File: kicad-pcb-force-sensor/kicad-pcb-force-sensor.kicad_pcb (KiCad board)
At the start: 2 copper layers, 68.6 x 53.3 mm, 24 parts, among them J1 Power, J2 Digital/PWM, J3 Analog, J4 Digital/PWM, U3 KY-040

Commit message: Servo
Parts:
- added M1: Motor_Servo, graphite_emprunts:Servo, F.Cu at (104.0, 50.9)
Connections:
- J2 pad 9: /D9 -> D9 PWM

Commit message: Avec pistes
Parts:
- removed R2: 1k, Resistor_THT:R_Axial_DIN0204_L3.6mm_D1.6mm_P7.62mm_Horizontal
- AOP1: value LTC1050HS8_PBF -> LTC1050
- Rflex1: value 23k -> 47k
- moved Flex_sensor1 52.3 mm to (157.3, 90.6), turned to -90 degrees
- moved U1 46.3 mm to (145.3, 59.0), turned to 0 degrees
- moved Pot_Digital1 41.7 mm to (113.9, 66.1), turned to -90 degrees
- moved Rflex1 41.3 mm to (151.0, 73.6), turned to 90 degrees
- moved M1 29.3 mm to (132.0, 59.5), turned to 180 degrees
- moved C2 25.7 mm to (139.2, 81.5)
- moved R6 24.4 mm to (145.5, 72.7), turned to -90 degrees
- moved Graphite_sensor1 23.9 mm to (137.0, 93.5)
- moved C1 22.7 mm to (134.8, 81.5), turned to 180 degrees
- moved R1 22.4 mm to (126.4, 86.5)
- moved C4 21.0 mm to (137.8, 72.0), turned to 180 degrees
- moved AOP1 20.9 mm to (122.5, 74.5), turned to 90 degrees
- moved U3 20.8 mm to (159.0, 61.7), turned to -90 degrees
- moved R5 18.8 mm to (138.6, 90.0), turned to 180 degrees
- moved R3 8.77 mm to (130.2, 77.0)
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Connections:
- J2 pad 8: D10 PWM/MOSI -> D10 PWM/SS
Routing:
- net VCC: track 0.00 -> 214.4 mm
- net R2: track 0.00 -> 48.4 mm
- net D11 PWM/MOSI: track 0.00 -> 34.7 mm
- net Net-(AOP1-OUT): track 0.00 -> 33.7 mm
- net Flex: track 0.00 -> 29.1 mm
- net DT: track 0.00 -> 26.6 mm
- net ADC: track 0.00 -> 23.6 mm
- net Net-(AOP1-+IN): track 0.00 -> 20.8 mm
- net D10 PWM/SS: track 0.00 -> 20.2 mm
- net D13 PWM/SCK: track 0.00 -> 15.9 mm
- net SCL: track 0.00 -> 15.7 mm
- net GND: track 0.00 -> 13.9 mm
- net SW: track 0.00 -> 13.6 mm
- net D9 PWM: track 0.00 -> 12.3 mm
- net TXD: track 0.00 -> 11.8 mm
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- added copper zone on B.Cu, net GND
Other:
- board size 68.6 x 53.3 mm -> 68.8 x 55 mm
- board text added: "SCL"

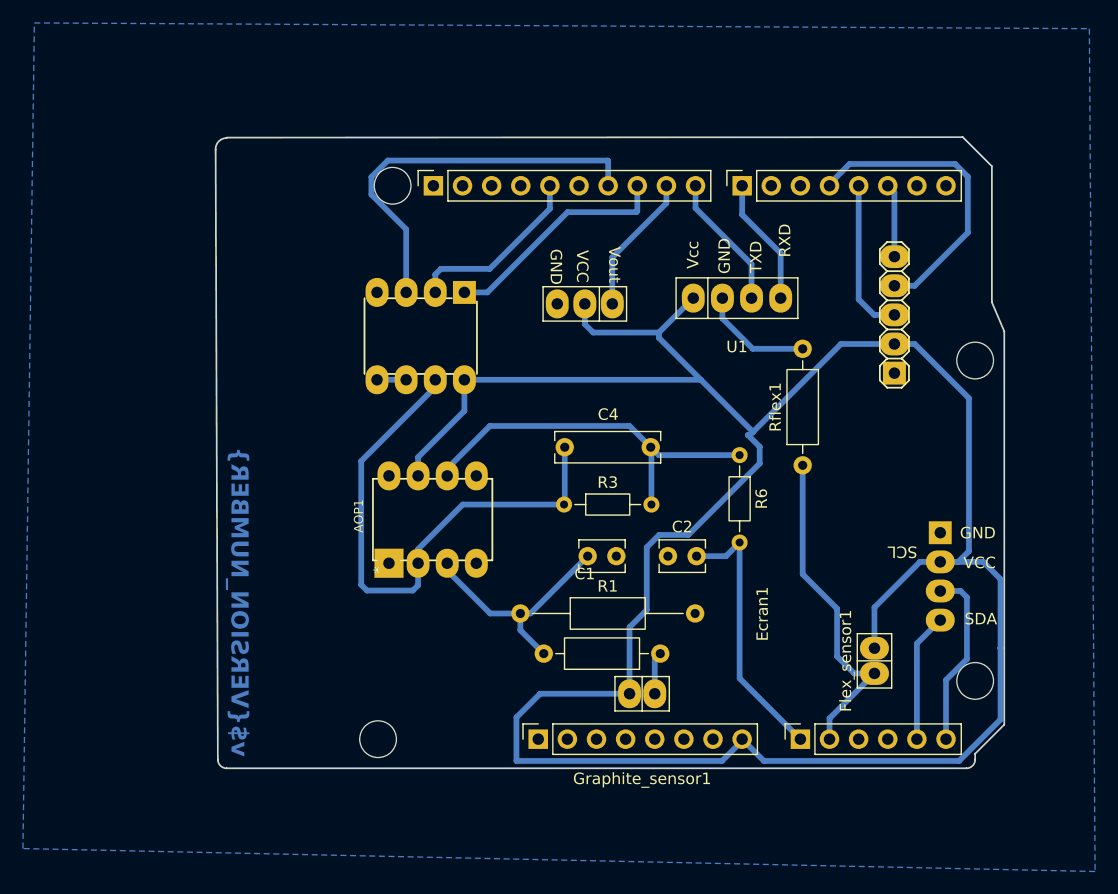
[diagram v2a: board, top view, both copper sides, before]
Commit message: Modifier pins à 0.8mm plus détails
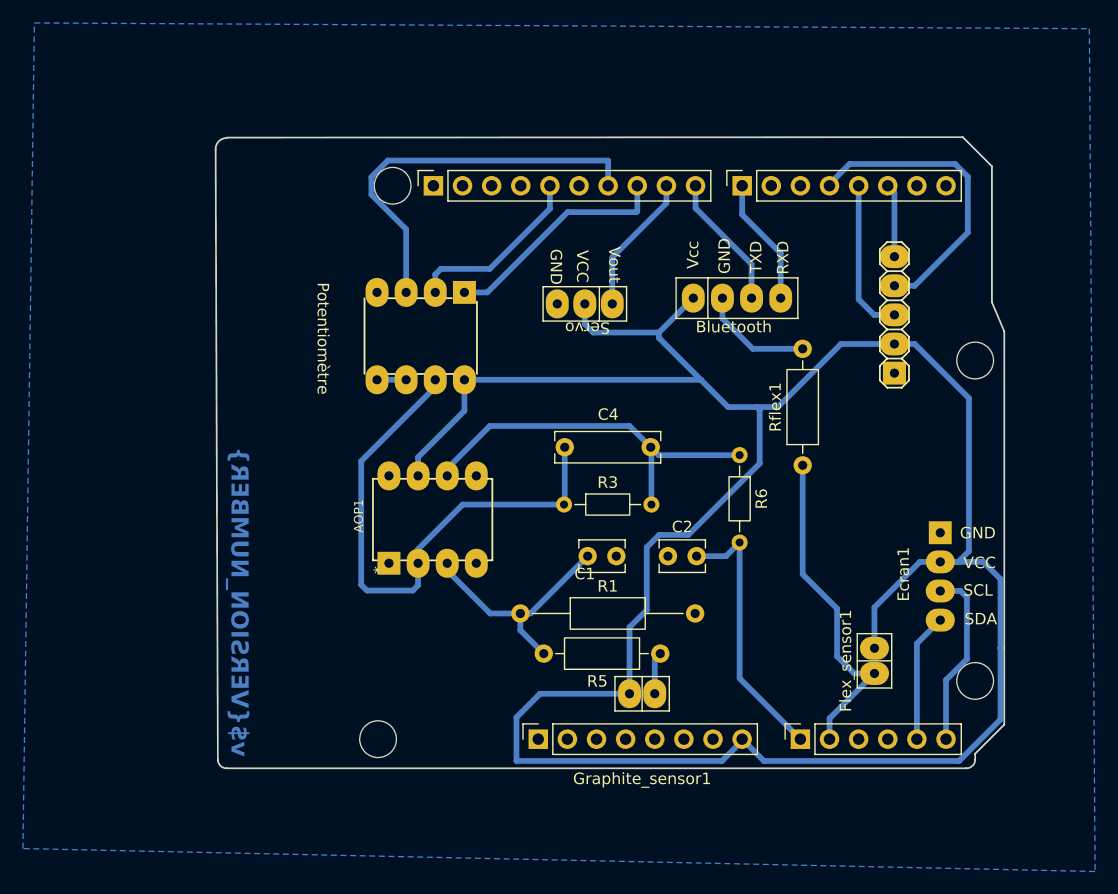
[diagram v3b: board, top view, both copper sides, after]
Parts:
- AOP1: value LTC1050 -> LTC1050HS8_PBF
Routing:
- net GND: track 13.9 -> 12.9 mm
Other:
- board text removed: "RXD"
- board text removed: "SCL"

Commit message: GND y pins header arduino
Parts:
- moved C2 1.41 mm to (140.2, 82.5)
- moved Graphite_sensor1 1.35 mm to (135.7, 93.4)
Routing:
- net GND: track 12.9 -> 92.3 mm
- net VCC: track 214.2 -> 179.0 mm
- net Net-(Graphite_sensor1--): track 3.70 -> 5.53 mm
- net Net-(AOP1-OUT): track 33.7 -> 35.5 mm
- net ADC: track 23.6 -> 23.0 mm
